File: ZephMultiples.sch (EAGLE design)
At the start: 45 parts, among them IC1 TL074D, IC2 TL074D

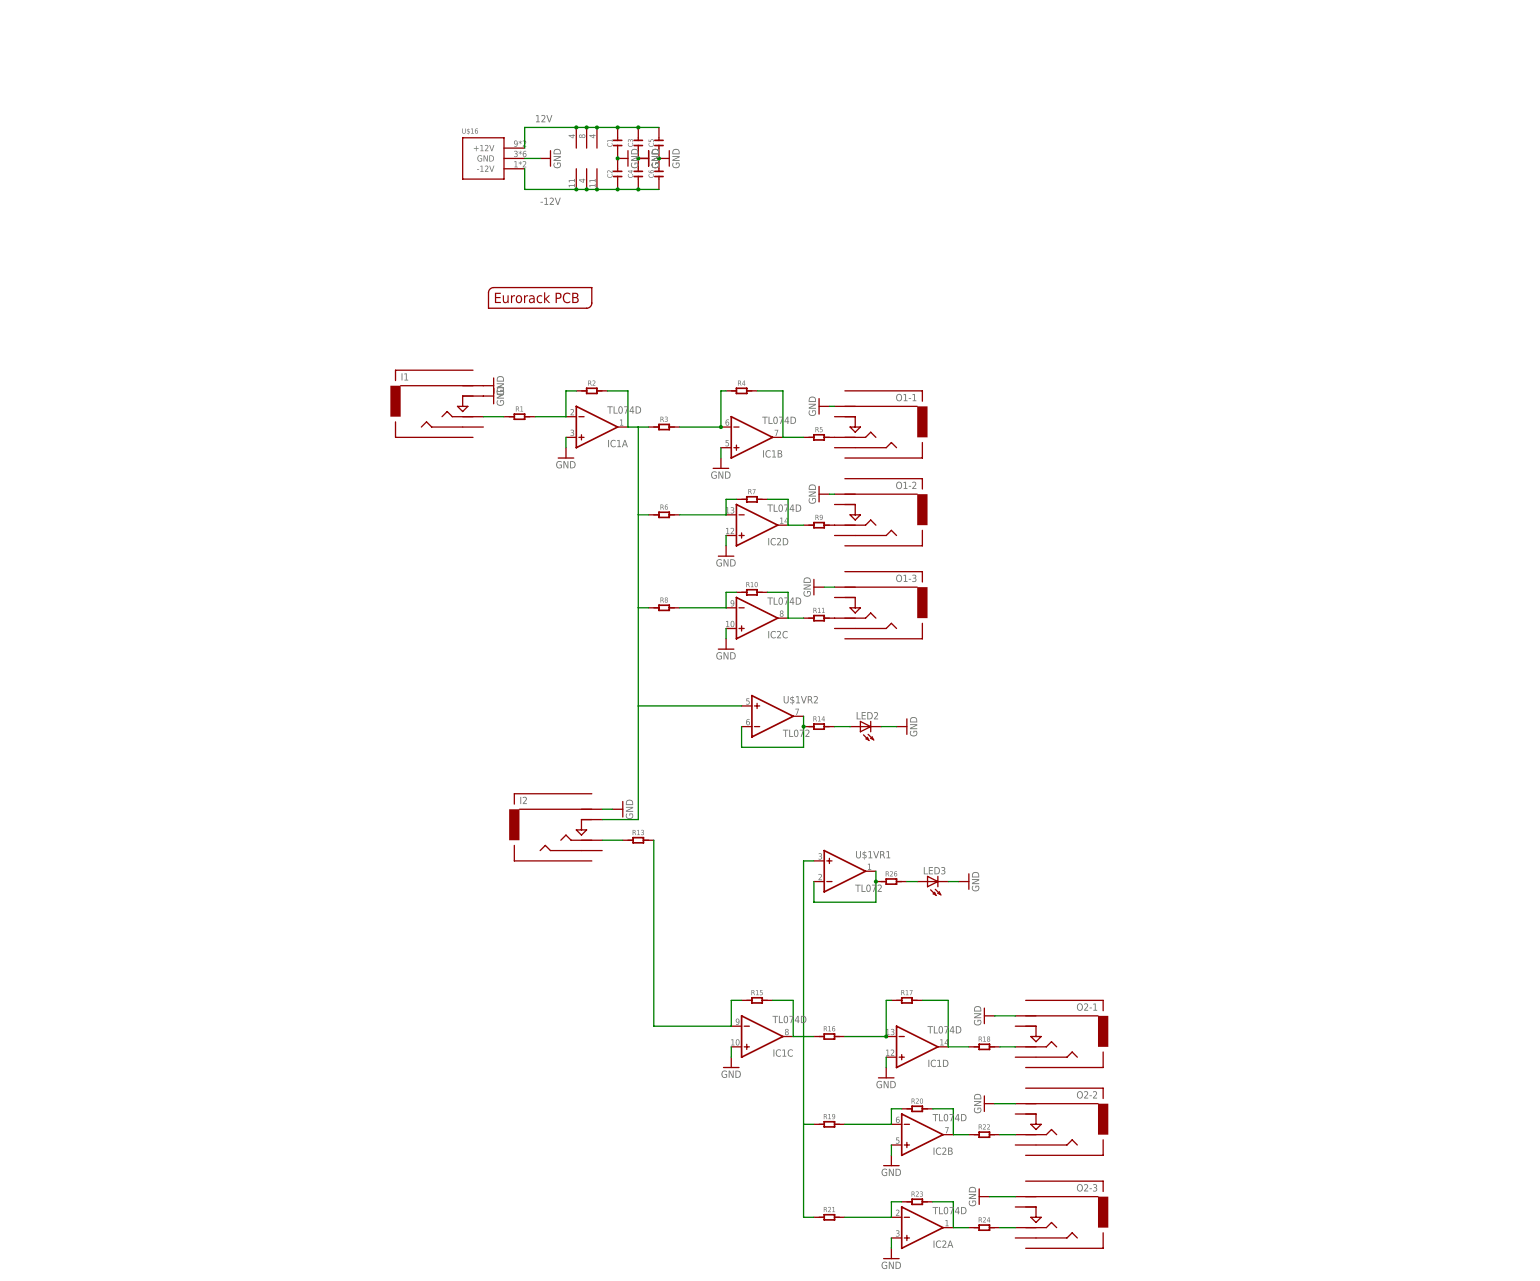
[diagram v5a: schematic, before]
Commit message: DRC & ERC on all boards = green now.
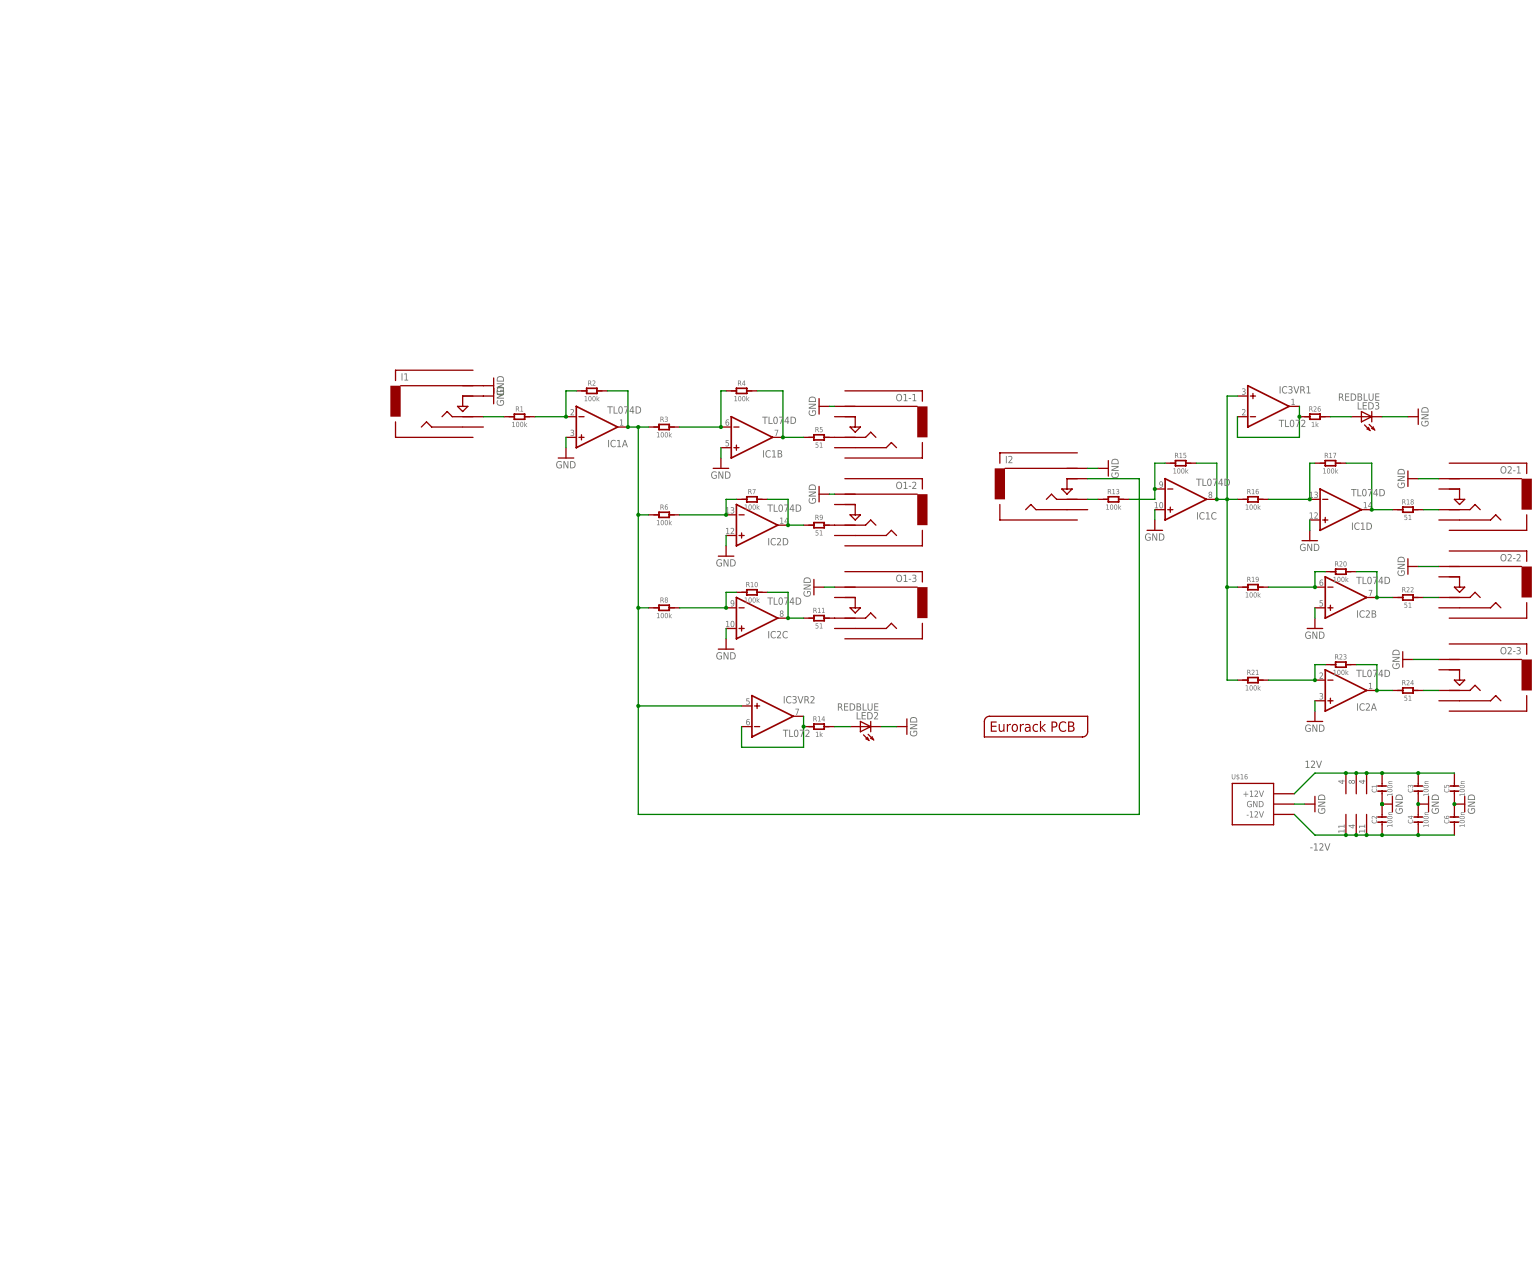
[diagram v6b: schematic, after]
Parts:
- removed U$1: TL072, EurorackModularParts:TL072
- added IC3: TL072, EurorackModularParts:TL072
- C1, C2, C3, C4, C5, C6: value (none) -> 100n
- LED2, LED3: value (none) -> REDBLUE
- R1, R10, R13, R15, R16, R17, R19, R2, R20, R21, R23, R3, R4, R6, R7, R8: value (none) -> 100k
- R11, R18, R22, R24, R5, R9: value (none) -> 51
- R14, R26: value (none) -> 1k
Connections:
- net -12V: now also IC3VR3.V-; no longer U$1VR3.V-
- net 12V: now also IC3VR3.V+; no longer U$1VR3.V+
- net N$16: now also IC3VR1.+IN; no longer U$1VR1.+IN
- net N$27: now also IC3VR2.-IN, IC3VR2.OUT; no longer U$1VR2.-IN, U$1VR2.OUT
- net N$28: now also IC3VR1.-IN, IC3VR1.OUT; no longer U$1VR1.-IN, U$1VR1.OUT
- net N$3: now also IC3VR2.+IN; no longer U$1VR2.+IN
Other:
- moved on the sheet: C1, C2, C3, C4, C5, C6, I2, IC1C, IC1D, IC2A, IC2B, LED3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
